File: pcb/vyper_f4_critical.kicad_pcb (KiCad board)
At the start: 4 copper layers, 30 x 64 mm, 81 parts, among them J1 USB_SERVICE_SH1.0_4P, J2 ESC_SH1.0_8P, J3 RX_UART1, J4 GPS_UART3, J5 EXTERNAL_I2C, J6 VTX_UART6, J7 SWD, J8 BEEPER_PAD, U1 STM32F405RGTx, U2 ICM-42688-P, U3 TPS54360DDA, U4 AP2112K-3.3, U5 AP2112K-3.3, U6 W25Q128JVS, U7 BMP280, U8 SN74AHCT1G125DBVR, Y1 8MHz 10pF

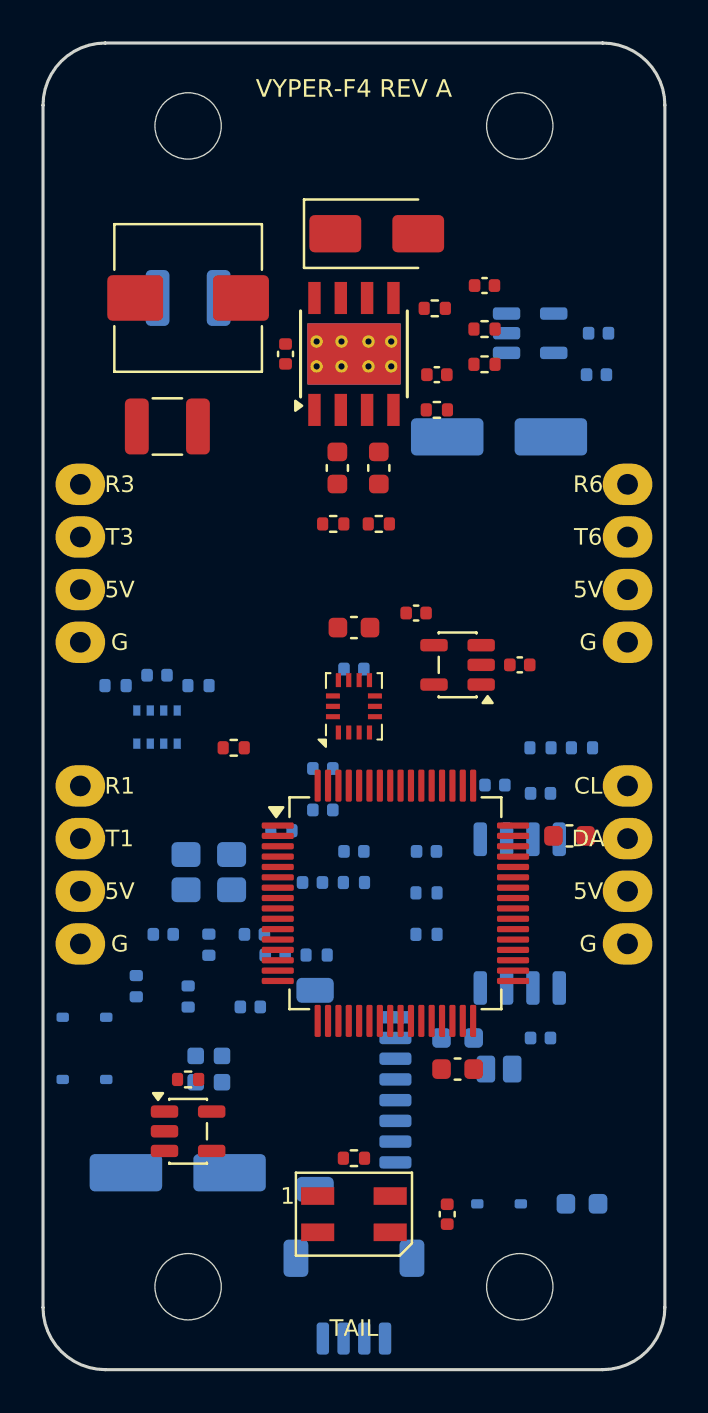
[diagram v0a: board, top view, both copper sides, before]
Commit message: Route Vyper FC power gyro bus and clock
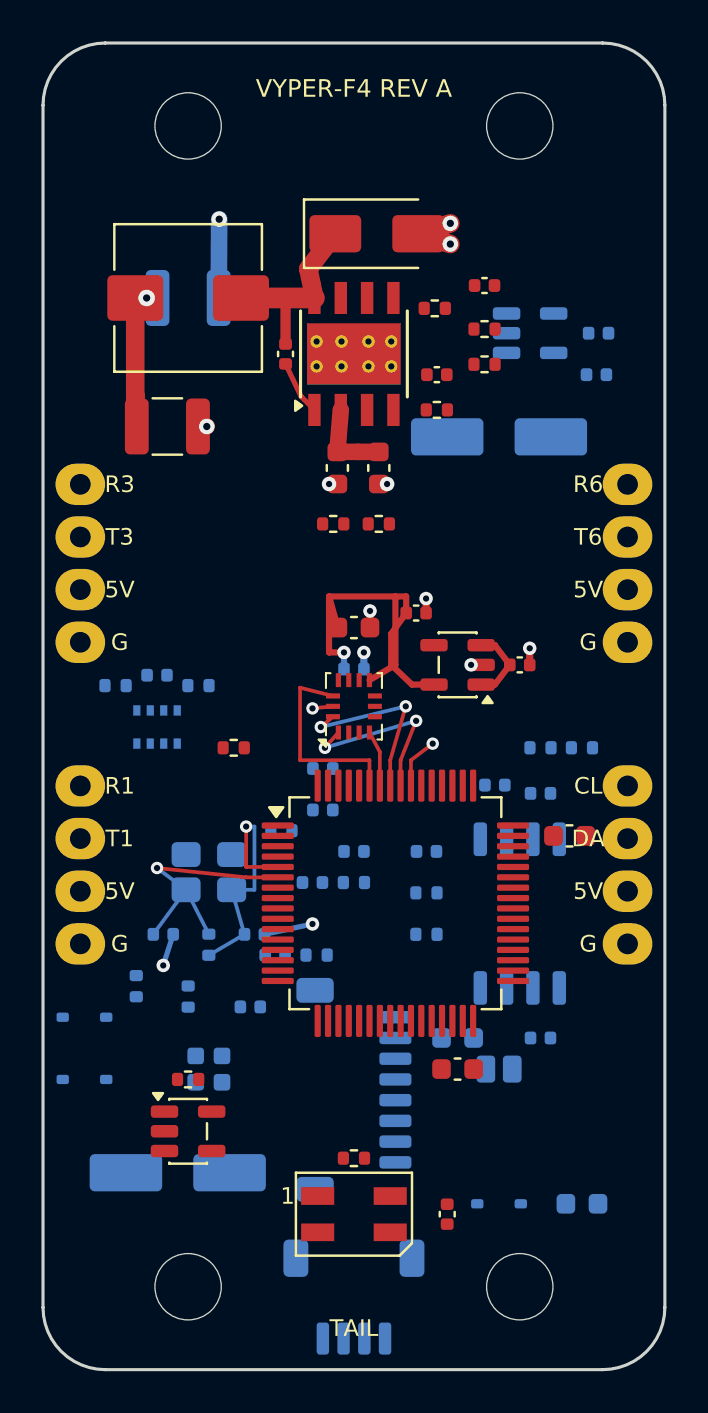
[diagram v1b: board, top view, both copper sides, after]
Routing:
- net V3V3_GYRO: track 0.00 -> 20.2 mm, vias 0 -> 1
- net GND: track 0.00 -> 15.8 mm, vias 0 -> 13
- net HSE_OUT: track 0.00 -> 12.7 mm, vias 0 -> 1
- net HSE_IN: track 0.00 -> 12.3 mm, vias 0 -> 1
- net BUCK_SW: track 0.00 -> 10.7 mm
- net GYRO_CS: track 0.00 -> 9.71 mm
- net SPI1_SCK: track 0.00 -> 9.58 mm, vias 0 -> 2
- net SPI1_MOSI: track 0.00 -> 8.92 mm, vias 0 -> 2
- net SPI1_MISO: track 0.00 -> 8.84 mm, vias 0 -> 2
- net V5_BUCK: track 0.00 -> 7.28 mm, vias 0 -> 1
- net VBAT_6S: track 0.00 -> 4.03 mm
- net LOGIC_IN: track 0.00 -> 3.71 mm
- net GYRO_INT1: track 0.00 -> 2.69 mm
- net BUCK_BOOT: track 0.00 -> 2.66 mm
- added copper zone on In1.Cu, net GND

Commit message: Route STM32 VCAP regulator networks
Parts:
- moved C19 0.43 mm to (5.25, 17.9), turned to -90 degrees
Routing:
- net GND: track 15.8 -> 18.1 mm, vias 13 -> 15
- net VCAP2: track 0.00 -> 1.95 mm
- net VCAP1: track 0.00 -> 1.90 mm

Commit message: Route Vyper FC logic and analog supply planes
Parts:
- C12, C13: moved to F.Cu
- moved FB1 9.75 mm to (-5.80, 11.8), turned to 90 degrees
- moved C12 9.70 mm to (-7.40, 10.7), turned to 180 degrees
- moved C13 9.15 mm to (-7.40, 12.0), turned to 180 degrees
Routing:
- net GND: track 18.1 -> 28.1 mm, vias 15 -> 19
- net V3V3_A: track 0.00 -> 4.76 mm
- net V3V3: track 0.00 -> 2.87 mm, vias 0 -> 2
- added copper zone on In2.Cu, net V3V3

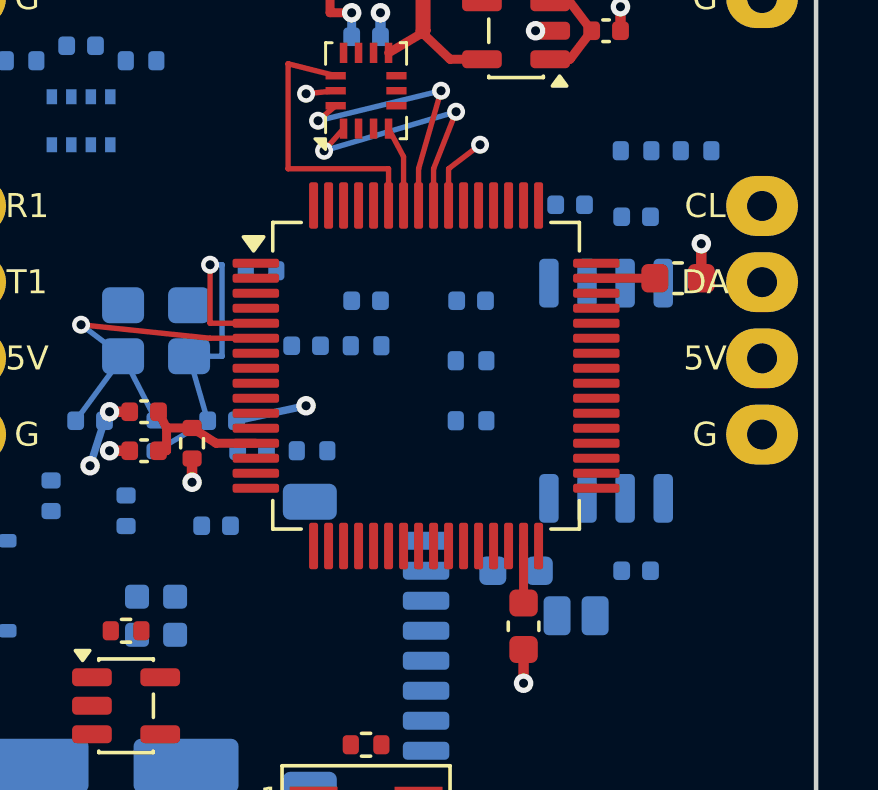
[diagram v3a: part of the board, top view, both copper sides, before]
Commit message: Complete Vyper FC MCU power fanout
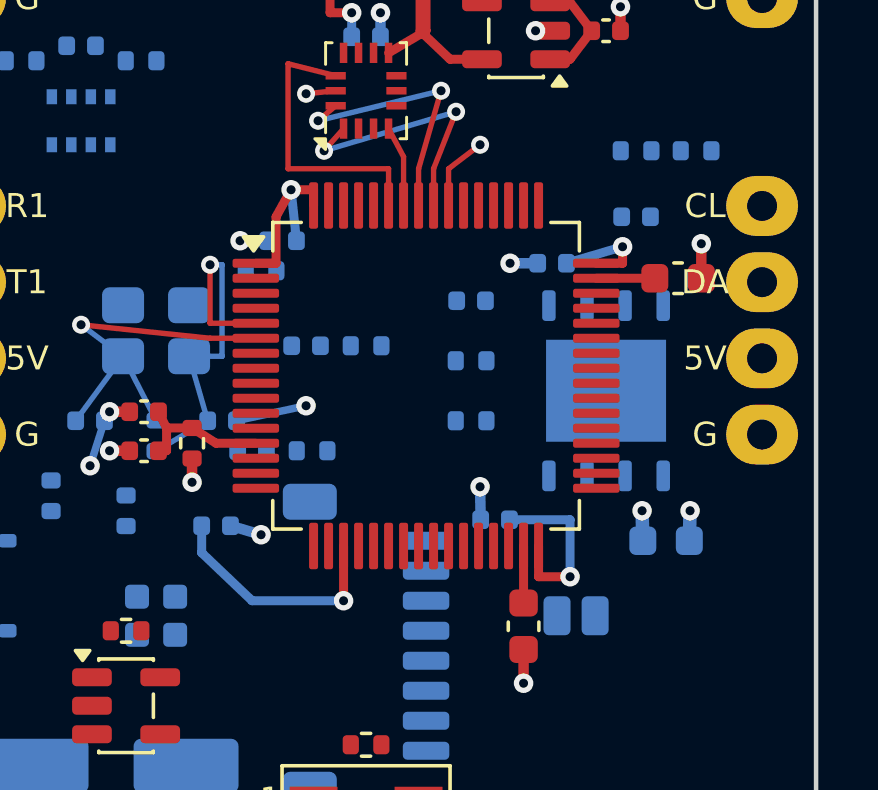
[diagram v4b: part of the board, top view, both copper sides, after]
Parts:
- U6: value W25Q128JVS -> W25Q128JVPIM; footprint SOIC-8_5.3x5.3mm_P1.27mm -> WDFN-8-1EP_6x5mm_P1.27mm_EP3.4x4mm
- moved C18 5.10 mm to (10.0, 15.0)
- moved C16 5.00 mm to (4.30, 14.3), turned to 180 degrees
- moved C14 3.44 mm to (-2.80, 5.00), turned to 180 degrees
- moved C15 2.04 mm to (6.20, 5.75), turned to 180 degrees
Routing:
- net V3V3: track 2.87 -> 27.6 mm, vias 2 -> 7
- net GND: track 28.1 -> 33.1 mm, vias 19 -> 24

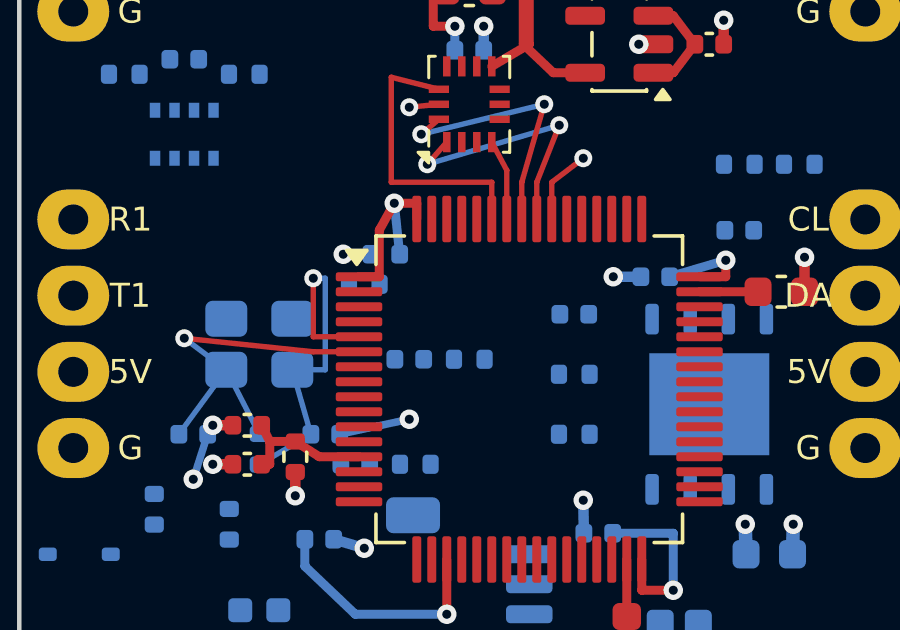
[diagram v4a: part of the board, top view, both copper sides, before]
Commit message: Route Vyper FC startup networks
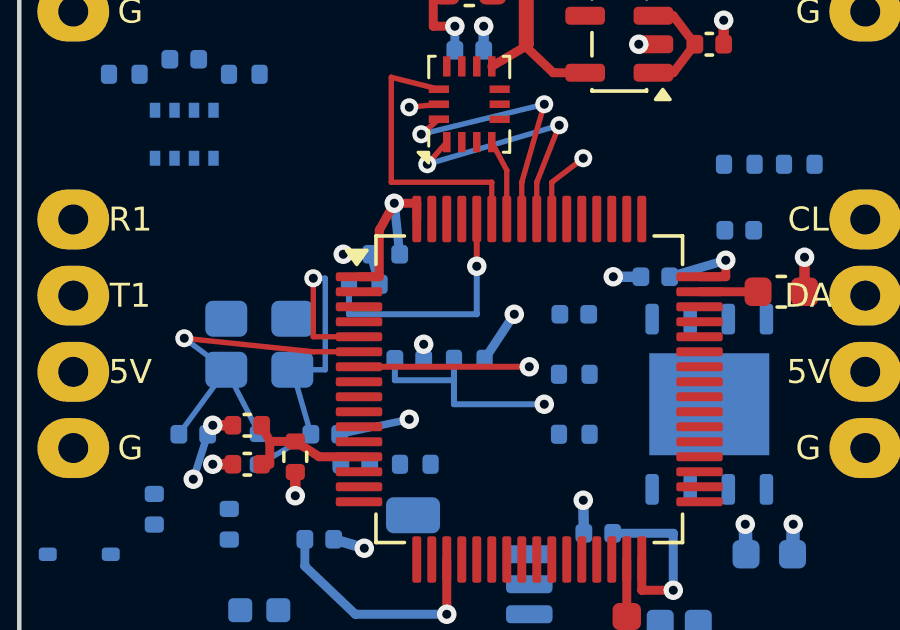
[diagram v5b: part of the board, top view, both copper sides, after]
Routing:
- net NRST: track 0.00 -> 14.2 mm, vias 0 -> 2
- net BOOT0: track 0.00 -> 8.43 mm, vias 0 -> 1
- net V3V3: track 27.6 -> 29.4 mm, vias 7 -> 8
- net GND: track 33.1 -> 34.7 mm, vias 24 -> 25

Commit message: Specify exact FC USB protection
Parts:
- removed D5, D6: PESD5V low-C, D_SOD-323
- added U9: USBLC6-2SC6, SOT-666, F.Cu at (0.00, 21.5)
- R14, R15: moved to F.Cu
- moved R15 21.7 mm to (10.6, 8.30)
- moved R14 18.2 mm to (9.30, 8.30)
- moved C31 11.5 mm to (-7.00, 24.5)
- moved R19 4.55 mm to (-4.50, 22.5)
- moved D4 2.50 mm to (-2.00, 26.0)
- moved C28 0.50 mm to (10.5, 24.0), turned to 90 degrees
- turned D7 to 180 degrees

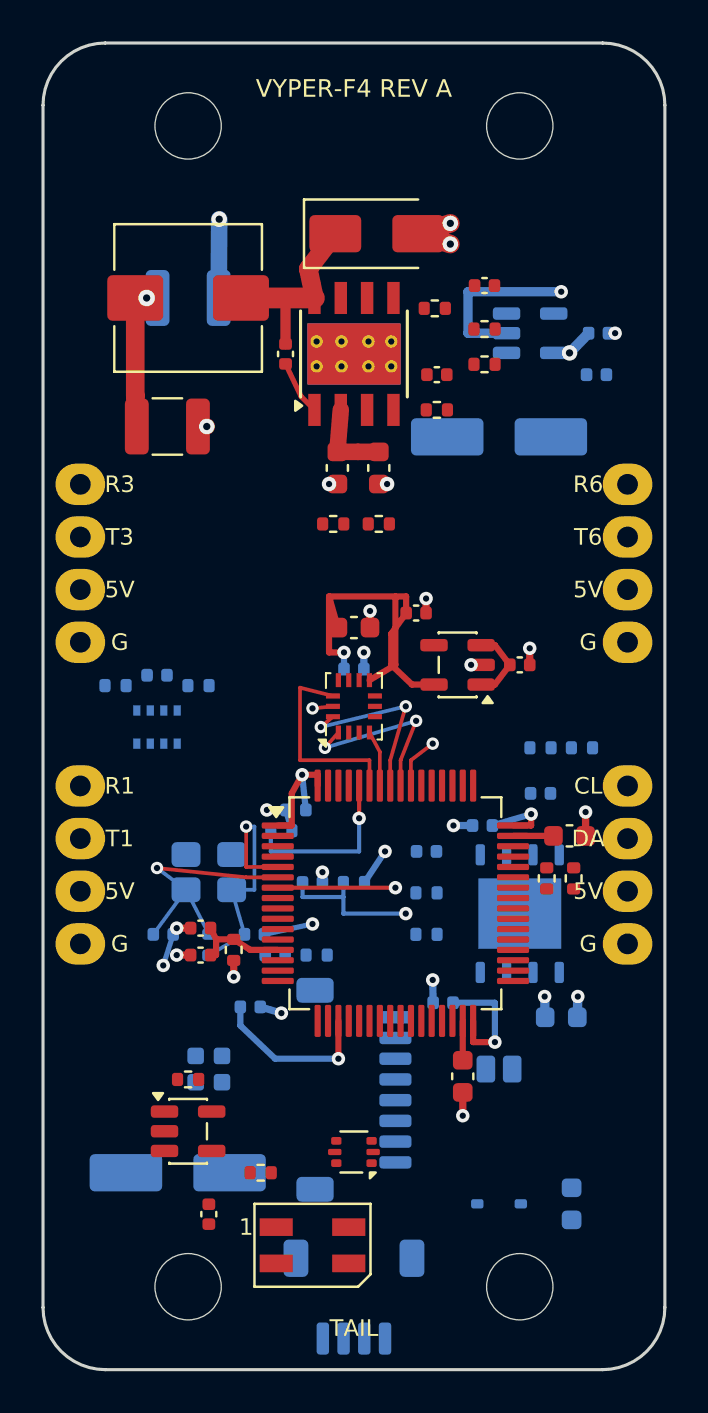
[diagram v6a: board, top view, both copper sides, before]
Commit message: Route and match Vyper FC USB
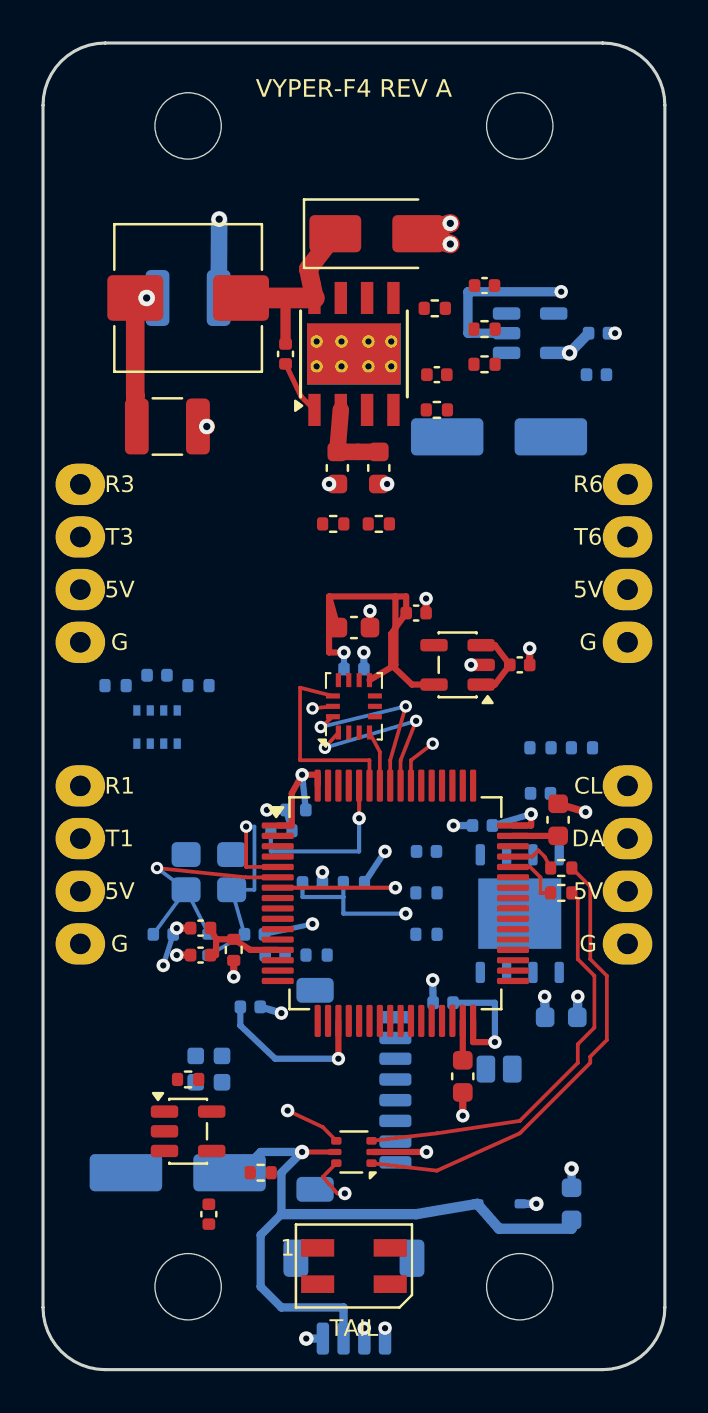
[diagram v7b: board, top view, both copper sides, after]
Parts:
- R14, R15: value 22R -> ERJ2RKF22R0X 22R 1%
- moved D4 2.24 mm to (0.00, 27.0)
- moved R14 0.99 mm to (10.0, 9.00), turned to 180 degrees
- moved C20 0.95 mm to (9.85, 5.47), turned to 90 degrees
- moved R15 0.78 mm to (10.0, 7.80), turned to 180 degrees
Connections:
- J1 pad 3: USB_DM_RAW -> USB_DP_RAW
- J1 pad 4: USB_DP_RAW -> USB_DM_RAW
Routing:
- net USB_DP_RAW: track 0.00 -> 36.0 mm, vias 0 -> 2
- net USB_DM_RAW: track 0.00 -> 35.9 mm, vias 0 -> 2
- net USB_5V: track 0.00 -> 33.7 mm, vias 0 -> 1
- net GND: track 34.7 -> 39.9 mm, vias 25 -> 29
- net USB_DM: track 0.00 -> 2.77 mm
- net USB_DP: track 0.00 -> 2.40 mm
